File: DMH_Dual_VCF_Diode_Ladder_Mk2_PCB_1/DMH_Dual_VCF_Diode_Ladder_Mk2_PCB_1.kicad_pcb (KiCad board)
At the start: 2 copper layers, 146 x 175 mm, 201 parts, among them J0 Conn_01x01, J100 IDC_02x08, J50 Conn_01x06, J60 Conn_01x06, J70 Conn_01x06, J80 Conn_01x06, Q1 BC548, Q2 BC548, Q3 BC548, Q4 BC548, SW1 SW_SPDT, SW10 SW_DPDT_OnOn, SW2 SW_SPDT, SW3 SW_SPDT, SW4 SW_SPDT, SW5 SW_SPDT, SW6 SW_SPDT, SW7 SW_SPDT_OnOffOn, SW8 SW_SPDT_321, SW9 SW_SPDT_OnOffOn, U1 TL074, U2 TL074, U3 TL074, U4 TL074, U5 TL074, U6 TL074, U7 TL074

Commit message: PCB1 component placement in progress
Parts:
- removed D3: LED_Blue, LED_THT:LED_D3.0mm
- removed D4, D5: LED_Red, LED_THT:LED_D3.0mm
- removed J50, J60, J70, J80: Conn_01x06, Connector_PinSocket_2.54mm:PinSocket_1x06_P2.54mm_Vertical
- removed R1, R11, R16, R76: 100k, Resistor_THT:R_Axial_DIN0207_L6.3mm_D2.5mm_P7.62mm_Horizontal
- removed R10, R24, R25, R9: 47k, Resistor_THT:R_Axial_DIN0207_L6.3mm_D2.5mm_P7.62mm_Horizontal
- removed R12, R17, R2: 27k, Resistor_THT:R_Axial_DIN0207_L6.3mm_D2.5mm_P7.62mm_Horizontal
- removed R13, R14, R15: 3k3, Resistor_THT:R_Axial_DIN0207_L6.3mm_D2.5mm_P7.62mm_Horizontal
- removed R23, R8: 68k, Resistor_THT:R_Axial_DIN0207_L6.3mm_D2.5mm_P7.62mm_Horizontal
- removed R80: 20k, Resistor_THT:R_Axial_DIN0207_L6.3mm_D2.5mm_P7.62mm_Horizontal
- removed RV1, RV18, RV22, RV6, RV7: 100k, SynthStuff:Potentiometer_Alpha_RD901F-40-00D_Single_Vertical
- removed RV11, RV16, RV20, RV3, RV5, RV9: 100k, SynthStuff:Potentiometer_TT_P110KH1
- removed RV19: 100k, Potentiometer_THT:Potentiometer_Bourns_3296W_Vertical
- removed SW1, SW2, SW3, SW4, SW5, SW6: SW_SPDT, SynthStuff:Toggle_Switch_TE
- removed SW10: SW_DPDT_OnOn, SynthStuff:Toggle_Switch_2_Poles_TE
- removed SW7, SW9: SW_SPDT_OnOffOn, SynthStuff:Toggle_Switch_TE
- removed SW8: SW_SPDT_321, SynthStuff:Toggle_Switch_TE
- added C19: 100nF, Capacitor_THT:C_Disc_D4.3mm_W1.9mm_P5.00mm, B.Cu at (265.6, 117.3)
- added C20: 100nF, Capacitor_THT:C_Disc_D4.3mm_W1.9mm_P5.00mm, B.Cu at (265.6, 120.8)
- added C35: 100nF, Capacitor_THT:C_Disc_D4.3mm_W1.9mm_P5.00mm, B.Cu at (265.6, 124.2)
- added C36: 100nF, Capacitor_THT:C_Disc_D4.3mm_W1.9mm_P5.00mm, B.Cu at (265.6, 127.7)
- added J1: TS_Jack_6.35mm_Sw, SynthStuff:CUI_MJ-63052A, F.Cu at (33.5, 190.2)
- added J10: TS_Jack_6.35mm_Sw, SynthStuff:CUI_MJ-63052A, F.Cu at (150.0, 208.8)
- added J11: TS_Jack_6.35mm_Sw, SynthStuff:CUI_MJ-63052A, F.Cu at (133.5, 190.2)
- added J12: TS_Jack_6.35mm_Sw, SynthStuff:CUI_MJ-63052A, F.Cu at (133.5, 208.8)
- added J13: TS_Jack_6.35mm_Sw, SynthStuff:CUI_MJ-63052A, F.Cu at (117.0, 208.8)
- added J14: TS_Jack_6.35mm_Sw, SynthStuff:CUI_MJ-63052A, F.Cu at (166.5, 208.8)
- added J15: Conn_01x08_PinHeader, Connector_PinHeader_2.54mm:PinHeader_1x08_P2.54mm_Vertical, F.Cu at (30.0, 128.0)
- added J16: Conn_01x08_PinHeader, Connector_PinHeader_2.54mm:PinHeader_1x08_P2.54mm_Vertical, F.Cu at (170.0, 128.0)
- added J17: Conn_01x06_PinHeader, Connector_PinHeader_2.54mm:PinHeader_1x06_P2.54mm_Vertical, F.Cu at (30.0, 94.5)
- added J18: Conn_01x06_PinHeader, Connector_PinHeader_2.54mm:PinHeader_1x06_P2.54mm_Vertical, F.Cu at (170.0, 94.5)
- added J19: Conn_01x04_PinHeader, Connector_PinHeader_2.54mm:PinHeader_1x04_P2.54mm_Vertical, F.Cu at (98.0, 143.8)
- added J2: TS_Jack_6.35mm_Sw, SynthStuff:CUI_MJ-63052A, F.Cu at (50.0, 190.2)
- added J20: Conn_01x04_PinHeader, Connector_PinHeader_2.54mm:PinHeader_1x04_P2.54mm_Vertical, F.Cu at (102.0, 143.8)
- added J200: IDC_02x05, SynthStuff:IDC-Header_2x05_P2.54mm_Vertical_BackBone, B.Cu at (81.9, 192.2)
- added J21: Conn_01x06_PinHeader, Connector_PinHeader_2.54mm:PinHeader_1x06_P2.54mm_Vertical, F.Cu at (30.0, 56.5)
- added J210: IDC_02x05, SynthStuff:IDC-Header_2x05_P2.54mm_Vertical_BackBone, B.Cu at (108.0, 192.2)
- added J22: Conn_01x06_PinHeader, Connector_PinHeader_2.54mm:PinHeader_1x06_P2.54mm_Vertical, F.Cu at (170.0, 56.5)
- added J23: Conn_01x04_PinHeader, Connector_PinHeader_2.54mm:PinHeader_1x04_P2.54mm_Vertical, F.Cu at (96.2, 62.8)
- added J3: TS_Jack_6.35mm_Sw, SynthStuff:CUI_MJ-63052A, F.Cu at (50.0, 208.8)
- added J4: TS_Jack_6.35mm_Sw, SynthStuff:CUI_MJ-63052A, F.Cu at (66.5, 190.2)
- added J5: TS_Jack_6.35mm_Sw, SynthStuff:CUI_MJ-63052A, F.Cu at (66.5, 208.8)
- added J6: TS_Jack_6.35mm_Sw, SynthStuff:CUI_MJ-63052A, F.Cu at (83.0, 208.8)
- added J7: TS_Jack_6.35mm_Sw, SynthStuff:CUI_MJ-63052A, F.Cu at (33.5, 208.8)
- added J8: TS_Jack_6.35mm_Sw, SynthStuff:CUI_MJ-63052A, F.Cu at (166.5, 190.2)
- added J9: TS_Jack_6.35mm_Sw, SynthStuff:CUI_MJ-63052A, F.Cu at (150.0, 190.2)
- added Q5: BC548, Package_TO_SOT_THT:TO-92L_Inline_Wide, B.Cu at (297.4, 174.2)
- added Q6: BC548, Package_TO_SOT_THT:TO-92L_Inline_Wide, B.Cu at (297.5, 184.4)
- added Q7: BC548, Package_TO_SOT_THT:TO-92L_Inline_Wide, B.Cu at (254.5, 209.7)
- added Q8: BC548, Package_TO_SOT_THT:TO-92L_Inline_Wide, B.Cu at (254.7, 218.8)
- added R100: 10k, Resistor_THT:R_Axial_DIN0207_L6.3mm_D2.5mm_P7.62mm_Horizontal, B.Cu at (330.1, 170.2)
- added R101: 1k, Resistor_THT:R_Axial_DIN0207_L6.3mm_D2.5mm_P7.62mm_Horizontal, B.Cu at (330.1, 174.2)
- added R102: 10k, Resistor_THT:R_Axial_DIN0207_L6.3mm_D2.5mm_P7.62mm_Horizontal, B.Cu at (330.1, 178.2)
- added R103: 100k, Resistor_THT:R_Axial_DIN0207_L6.3mm_D2.5mm_P7.62mm_Horizontal, B.Cu at (330.1, 182.3)
- added R104: 33k, Resistor_THT:R_Axial_DIN0207_L6.3mm_D2.5mm_P7.62mm_Horizontal, B.Cu at (330.1, 186.3)
- added R105: 100k, Resistor_THT:R_Axial_DIN0207_L6.3mm_D2.5mm_P7.62mm_Horizontal, B.Cu at (319.4, 158.0)
- added R106: 100k, Resistor_THT:R_Axial_DIN0207_L6.3mm_D2.5mm_P7.62mm_Horizontal, B.Cu at (319.4, 162.1)
- added R107: 100k, Resistor_THT:R_Axial_DIN0207_L6.3mm_D2.5mm_P7.62mm_Horizontal, B.Cu at (319.4, 166.1)
- added R108: 100R, Resistor_THT:R_Axial_DIN0207_L6.3mm_D2.5mm_P7.62mm_Horizontal, B.Cu at (319.4, 170.2)
- added R109: 100R, Resistor_THT:R_Axial_DIN0207_L6.3mm_D2.5mm_P7.62mm_Horizontal, B.Cu at (319.4, 174.2)
- added R110: 10k, Resistor_THT:R_Axial_DIN0207_L6.3mm_D2.5mm_P7.62mm_Horizontal, B.Cu at (319.4, 178.2)
- added R112: 82k, Resistor_THT:R_Axial_DIN0207_L6.3mm_D2.5mm_P7.62mm_Horizontal, B.Cu at (319.4, 182.3)
- added R113: 100k, Resistor_THT:R_Axial_DIN0207_L6.3mm_D2.5mm_P7.62mm_Horizontal, B.Cu at (319.4, 186.3)
- added R114: 20k, Resistor_THT:R_Axial_DIN0207_L6.3mm_D2.5mm_P7.62mm_Horizontal, B.Cu at (287.3, 192.4)
- added R115: 20k, Resistor_THT:R_Axial_DIN0207_L6.3mm_D2.5mm_P7.62mm_Horizontal, B.Cu at (287.3, 196.4)
- added R116: 100k, Resistor_THT:R_Axial_DIN0207_L6.3mm_D2.5mm_P7.62mm_Horizontal, B.Cu at (287.3, 200.5)
- added R117: 10k, Resistor_THT:R_Axial_DIN0207_L6.3mm_D2.5mm_P7.62mm_Horizontal, B.Cu at (287.3, 204.6)
- added R118: 1k, Resistor_THT:R_Axial_DIN0207_L6.3mm_D2.5mm_P7.62mm_Horizontal, B.Cu at (287.3, 208.6)
- added R119: 10k, Resistor_THT:R_Axial_DIN0207_L6.3mm_D2.5mm_P7.62mm_Horizontal, B.Cu at (287.3, 212.7)
- added R120: 100k, Resistor_THT:R_Axial_DIN0207_L6.3mm_D2.5mm_P7.62mm_Horizontal, B.Cu at (287.3, 216.7)
- added R121: 33k, Resistor_THT:R_Axial_DIN0207_L6.3mm_D2.5mm_P7.62mm_Horizontal, B.Cu at (287.3, 220.8)
- added R122: 100k, Resistor_THT:R_Axial_DIN0207_L6.3mm_D2.5mm_P7.62mm_Horizontal, B.Cu at (276.5, 192.4)
- added R123: 100k, Resistor_THT:R_Axial_DIN0207_L6.3mm_D2.5mm_P7.62mm_Horizontal, B.Cu at (276.5, 196.4)
- added R124: 100k, Resistor_THT:R_Axial_DIN0207_L6.3mm_D2.5mm_P7.62mm_Horizontal, B.Cu at (276.5, 200.5)
- added R125: 100R, Resistor_THT:R_Axial_DIN0207_L6.3mm_D2.5mm_P7.62mm_Horizontal, B.Cu at (276.5, 204.6)
- added R126: 100R, Resistor_THT:R_Axial_DIN0207_L6.3mm_D2.5mm_P7.62mm_Horizontal, B.Cu at (276.5, 208.6)
- added R127: 10k, Resistor_THT:R_Axial_DIN0207_L6.3mm_D2.5mm_P7.62mm_Horizontal, B.Cu at (276.5, 212.7)
- added R129: 82k, Resistor_THT:R_Axial_DIN0207_L6.3mm_D2.5mm_P7.62mm_Horizontal, B.Cu at (276.5, 216.7)
- added R130: 100k, Resistor_THT:R_Axial_DIN0207_L6.3mm_D2.5mm_P7.62mm_Horizontal, B.Cu at (276.5, 220.8)
- added R97: 20k, Resistor_THT:R_Axial_DIN0207_L6.3mm_D2.5mm_P7.62mm_Horizontal, B.Cu at (330.1, 158.0)
- added R98: 20k, Resistor_THT:R_Axial_DIN0207_L6.3mm_D2.5mm_P7.62mm_Horizontal, B.Cu at (330.1, 162.1)
- added R99: 100k, Resistor_THT:R_Axial_DIN0207_L6.3mm_D2.5mm_P7.62mm_Horizontal, B.Cu at (330.1, 166.1)
- added RV24: 50k, Potentiometer_THT:Potentiometer_Bourns_3296W_Vertical, B.Cu at (302.1, 176.0)
- added RV26: 100k, Potentiometer_THT:Potentiometer_Bourns_3296W_Vertical, B.Cu at (302.1, 185.2)
- added RV29: 100k, Potentiometer_THT:Potentiometer_Bourns_3296W_Vertical, B.Cu at (259.2, 219.6)
- added U10: TL074, Package_DIP:DIP-14_W7.62mm_Socket, B.Cu at (153.8, 93.1)
- added U8: TL074, Package_DIP:DIP-14_W7.62mm_Socket, B.Cu at (153.8, 131.1)
- added U9: TL074, Package_DIP:DIP-14_W7.62mm_Socket, B.Cu at (53.8, 93.1)
- R62: value 33k -> 20k
- R65, R67: value 100k -> 10k
- R66: value 82k -> 1k
- R68, R70: value 100R -> 100k
- R69: value 10k -> 33k
- R72: value 20k -> 100k
- R73: value 20k -> 100R
- R74: value 10k -> 100R
- R77: value 100k -> 82k
- R78: value 1k -> 100k
- RV12, RV14: value 100k -> 50k; footprint SynthStuff:Potentiometer_Alpha_RD901F-40-00D_Single_Vertical -> Potentiometer_THT:Potentiometer_Bourns_3296W_Vertical; moved to B.Cu
- RV17: value 50k -> 100k
- moved D23 282.8 mm to (384.7, 59.2), turned to 180 degrees
- moved D22 280.9 mm to (384.7, 54.9), turned to 180 degrees
- moved D15 273.7 mm to (384.7, 24.7), turned to 180 degrees
- moved R48 263.4 mm to (373.9, 41.1), turned to 180 degrees
- moved R58 261.5 mm to (352.4, 33.0), turned to 180 degrees
- moved R46 261.2 mm to (373.9, 33.0)
- moved D7 260.5 mm to (285.1, 62.5), turned to 180 degrees
- moved R47 258.6 mm to (373.9, 37.1), turned to 180 degrees
- moved D8 256.7 mm to (285.1, 66.8), turned to 180 degrees
- moved C34 253.8 mm to (373.9, 69.6), turned to 180 degrees
- moved D9 252.9 mm to (285.1, 71.2), turned to 180 degrees
- moved R61 250.9 mm to (352.4, 45.2), turned to 180 degrees
- moved D10 249.2 mm to (285.1, 75.5), turned to 180 degrees
- moved R56 248.8 mm to (352.4, 24.9), turned to 180 degrees
- moved R52 246.6 mm to (363.1, 33.0), turned to 180 degrees
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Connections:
- net /CV Processing/Bus CV A Input renamed /Inputs and Outputs A/CV 3 TN
- C21 pad 1: Net-(C21-Pad1) -> /Core Circuit A/Input
- C28 pad 1: Net-(C28-Pad1) -> /Core Circuit B/Input
- D15 pad 2: /CV Processing/Link Switch -> /CV Processing/Link CV Switch
- R18 pad 2: Net-(U7A--) -> Net-(U8A--)
- R19 pad 2: Net-(U5B--) -> Net-(J16A-Pin_1)
- R20 pad 1: Net-(U5B--) -> Net-(J16A-Pin_1)
- R21 pad 2: Net-(U7B--) -> Net-(U8B--)
- R22 pad 2: Net-(U5B--) -> Net-(J16A-Pin_1)
- R4 pad 2: Net-(U5B--) -> Net-(J15A-Pin_1)
- R5 pad 1: Net-(U5B--) -> Net-(J15A-Pin_1)
- R62 pad 1: /Inputs and Outputs A/Res CV Jack -> Net-(Q1-C)
- R62 pad 2: Net-(U1D--) -> +12V
- R63 pad 1: Net-(R63-Pad1) -> Net-(Q2-C)
- R64 pad 2: Net-(U1B--) -> Net-(U1C--)
- R65 pad 1: Net-(R65-Pad1) -> Net-(U1C--)
- R65 pad 2: Net-(U1B--) -> Net-(Q1-C)
- R66 pad 1: Net-(U1B--) -> /Core Circuit A/Res Input
- R66 pad 2: Net-(R66-Pad2) -> Net-(R64-Pad1)
- R67 pad 1: Net-(Q1-B) -> Net-(U1C-+)
- R67 pad 2: /Core Circuit A/Raw Output -> Net-(Q2-C)
- R68 pad 1: GND -> Net-(U1C-+)
- R68 pad 2: Net-(Q1-B) -> GND
- R69 pad 1: Net-(R66-Pad2) -> /Inputs and Outputs A/Res CV Jack
- R69 pad 2: Net-(Q1-E) -> Net-(U1D--)
- R7 pad 2: Net-(U5B--) -> Net-(J15A-Pin_1)
- R70 pad 1: GND -> Net-(R70-Pad1)
- R70 pad 2: Net-(Q2-B) -> Net-(U1B--)
- R71 pad 1: Net-(R71-Pad1) -> Net-(Q1-B)
- R71 pad 2: Net-(Q2-B) -> /Core Circuit A/Raw Output
- R72 pad 1: Net-(Q1-C) -> Net-(R72-Pad1)
- R72 pad 2: +12V -> Net-(Q2-B)
- R73 pad 1: Net-(Q2-C) -> GND
- R73 pad 2: +12V -> Net-(Q1-B)
- R74 pad 1: Net-(U1C--) -> GND
- R74 pad 2: Net-(Q1-C) -> Net-(Q2-B)
- R75 pad 1: Net-(U1C-+) -> /Resonance A CV/Res CV
- R75 pad 2: Net-(Q2-C) -> Net-(Q1-E)
- R77 pad 1: Net-(R77-Pad1) -> Net-(U1B--)
- R77 pad 2: Net-(U1C--) -> /Resonance A CV/Res CV
- R78 pad 1: /Core Circuit A/Res Input -> Net-(J21C-Pin_3)
- R78 pad 2: Net-(R77-Pad1) -> Net-(U1B--)
- R83 pad 2: Net-(R83-Pad2) -> Net-(J22D-Pin_4)
- R86 pad 1: Net-(R83-Pad2) -> Net-(J22F-Pin_6)
- RV10 pad 1: Net-(U7B--) -> Net-(U8B--)
- RV12 pad 1: GND -> Net-(U10A--)
- RV12 pad 2: Net-(C21-Pad1) -> Net-(R122-Pad1)
- RV12 pad 3: /Core Circuit A/Input -> Net-(R122-Pad1)
- RV14 pad 1: GND -> Net-(U1D--)
- RV14 pad 2: Net-(C28-Pad1) -> Net-(R70-Pad1)
- RV14 pad 3: /Core Circuit B/Input -> Net-(R70-Pad1)
- RV17 pad 1: Net-(U1D--) -> -12V
- RV17 pad 2: Net-(R64-Pad1) -> Net-(R72-Pad1)
- RV17 pad 3: Net-(R64-Pad1) -> +12V
- RV8 pad 1: Net-(U7A--) -> Net-(U8A--)
- U1 pad 14: Net-(R64-Pad1) -> Net-(R70-Pad1)
- U1 pad 7: Net-(R66-Pad2) -> /Resonance A CV/Res CV
- U1 pad 8: Net-(R77-Pad1) -> Net-(R64-Pad1)
- U2 pad 8: Net-(R83-Pad2) -> Net-(J22D-Pin_4)
- U5 pad 7: /CV Processing/CV A -> Net-(U5B--)
- U6 pad 8: /CV Processing/CV B -> Net-(U6C--)
- U6 pad 9: Net-(U5B--) -> Net-(U6C--)
- U7 pad 1: Net-(R19-Pad1) -> /CV Processing/CV A
- U7 pad 2: Net-(U7A--) -> Net-(J15A-Pin_1)
- U7 pad 3: Net-(U7A-+) -> GND
- U7 pad 5: Net-(U7B-+) -> GND
- U7 pad 7: Net-(R22-Pad1) -> Net-(U7B--)
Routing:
- net +12V: track 550.6 -> 44.1 mm
- net -12V: track 494.0 -> 59.8 mm
- net Net-(U5B--): track 360.9 -> 0.00 mm
- net /Inputs and Outputs A/Res CV Jack: track 247.6 -> 4.71 mm
- net /Inputs and Outputs A/CV 3 TN: track 177.2 -> 2.54 mm
- net /Inputs and Outputs B/Res CV Jack: track 150.2 -> 0.00 mm
- net /Core Circuit A/Input: track 148.9 -> 0.00 mm
- net /CV Processing/CV2 A Input: track 147.5 -> 0.00 mm
- net Net-(D13-A): track 146.9 -> 0.00 mm
- net Net-(J22B-Pin_2): track 128.7 -> 0.00 mm
- net /CV Processing/CV B: track 117.8 -> 0.00 mm
- net /CV Processing/CV1 A Input: track 117.1 -> 0.00 mm
- net /CV Processing/Link Switch: track 115.9 -> 0.00 mm
- net /Core Circuit A/Output: track 113.9 -> 0.00 mm
- net /Core Circuit B/Output: track 113.8 -> 0.00 mm
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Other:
- outline, holes or cut-outs redrawn
- board text removed: "Mk1.0 - Month Year"

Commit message: Routed one half
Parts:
- moved R104 308.2 mm to (34.2, 100.2), turned to 0 degrees
- moved R103 307.8 mm to (29.2, 117.3), turned to 90 degrees
- moved R98 297.8 mm to (34.2, 128.5), turned to 0 degrees
- moved R113 297.0 mm to (34.2, 103.5), turned to 0 degrees
- moved R102 295.1 mm to (41.8, 115.5)
- moved R99 293.3 mm to (41.8, 112.2)
- moved R100 292.9 mm to (41.8, 118.8)
- moved R109 289.4 mm to (34.2, 125.2), turned to 0 degrees
- moved R107 288.6 mm to (34.2, 122.0), turned to 0 degrees
- moved R105 281.6 mm to (46.2, 89.5), turned to 0 degrees
- moved RV24 278.9 mm to (35.5, 94.2)
- moved R97 273.8 mm to (58.7, 122.0), turned to 0 degrees
- moved R110 272.0 mm to (53.8, 119.5)
- moved RV26 270.3 mm to (47.5, 94.2)
- moved R101 268.3 mm to (66.3, 125.2)
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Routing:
- net +12V: track 44.1 -> 404.0 mm
- net /Inputs and Outputs A/Res CV Jack: track 4.71 -> 243.3 mm
- net /Drive A/Input: track 0.00 -> 231.6 mm
- net -12V: track 59.8 -> 282.7 mm
- net /Drive A/Drive CV Input: track 0.00 -> 214.7 mm
- net /CV Processing/CV1 A Input: track 0.00 -> 186.1 mm
- net /CV Processing/CV2 A Input: track 0.00 -> 159.4 mm
- net /Core Circuit A/Output: track 0.00 -> 148.9 mm
- net /Inputs and Outputs A/CV 3 TN: track 2.54 -> 140.1 mm
- net Net-(D13-A): track 0.00 -> 114.6 mm
- net Net-(D10-A): track 0.00 -> 75.7 mm
- net /CV Processing/CV3 A Input: track 0.00 -> 74.6 mm
- net Net-(R107-Pad1): track 0.00 -> 65.1 mm
- net Net-(J19C-Pin_3): track 0.00 -> 64.9 mm
- net Net-(J19D-Pin_4): track 0.00 -> 62.8 mm
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
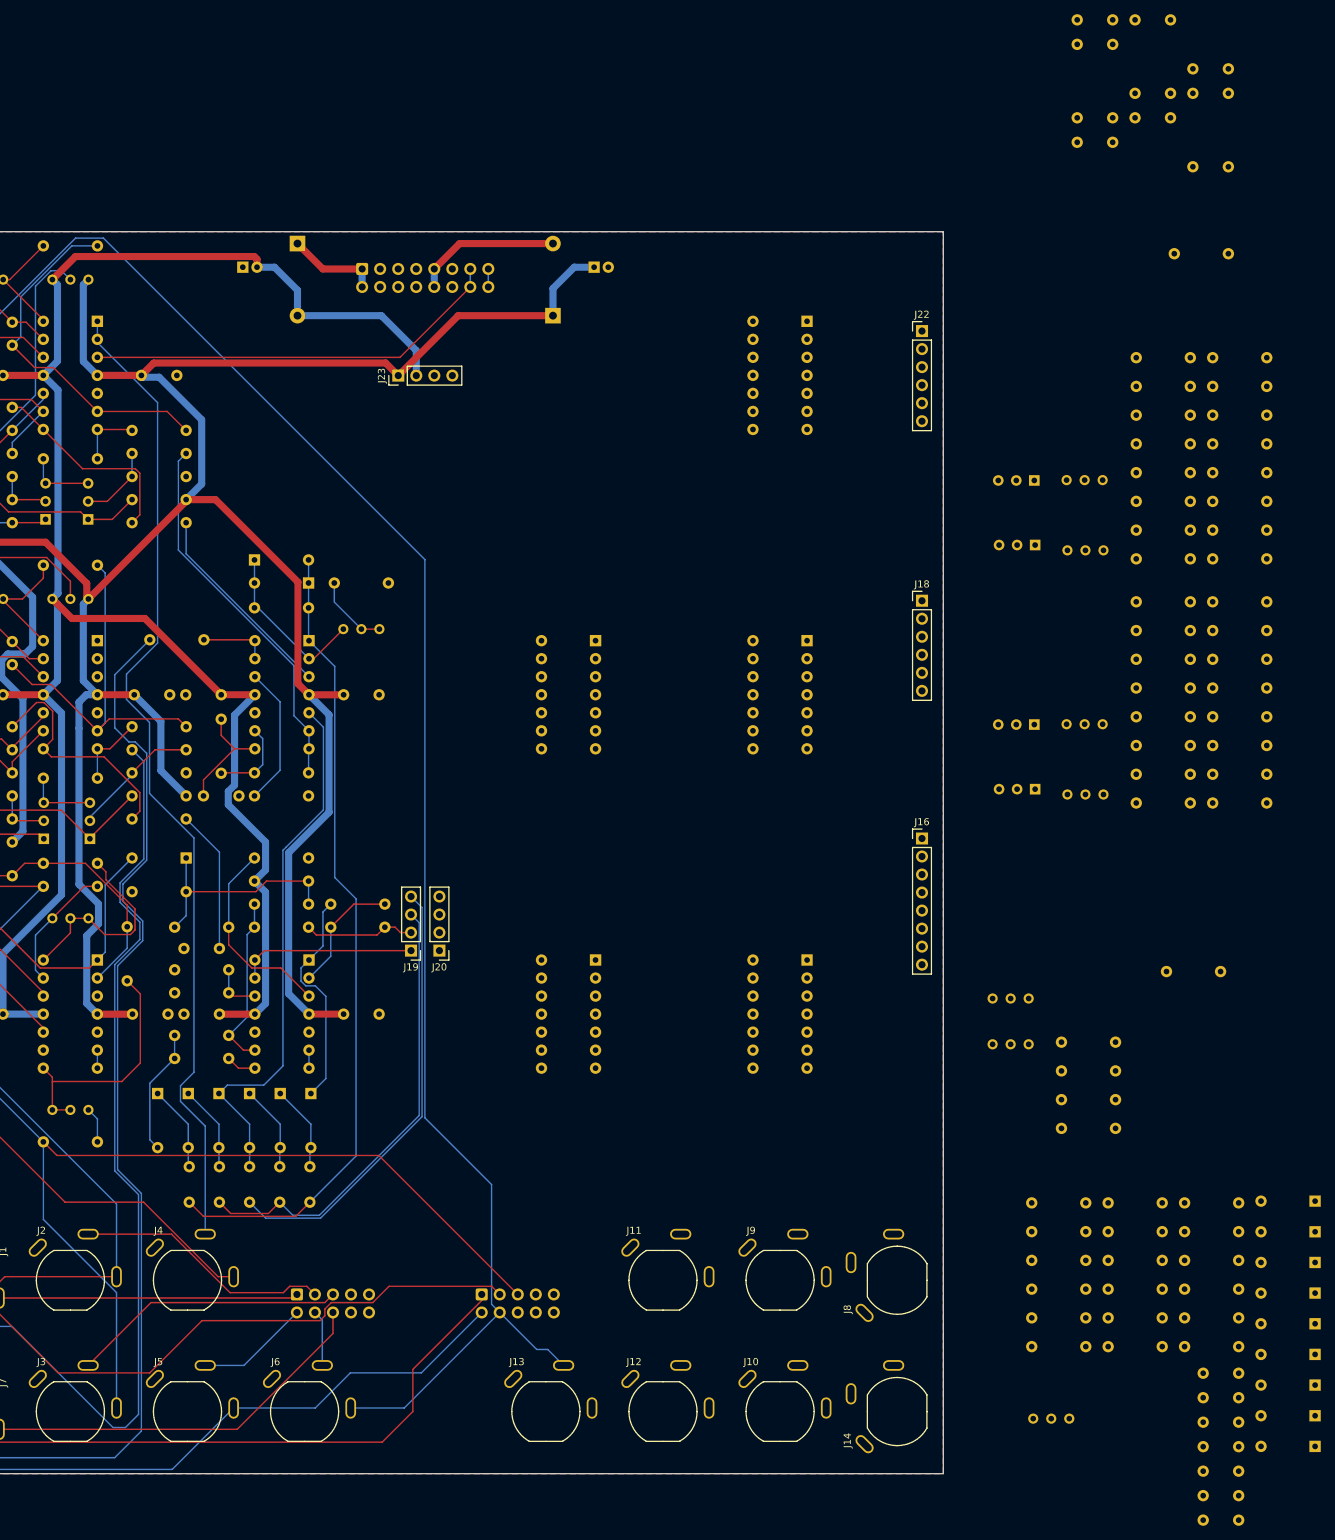
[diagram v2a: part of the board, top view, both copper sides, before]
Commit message: Placed components on circuit B
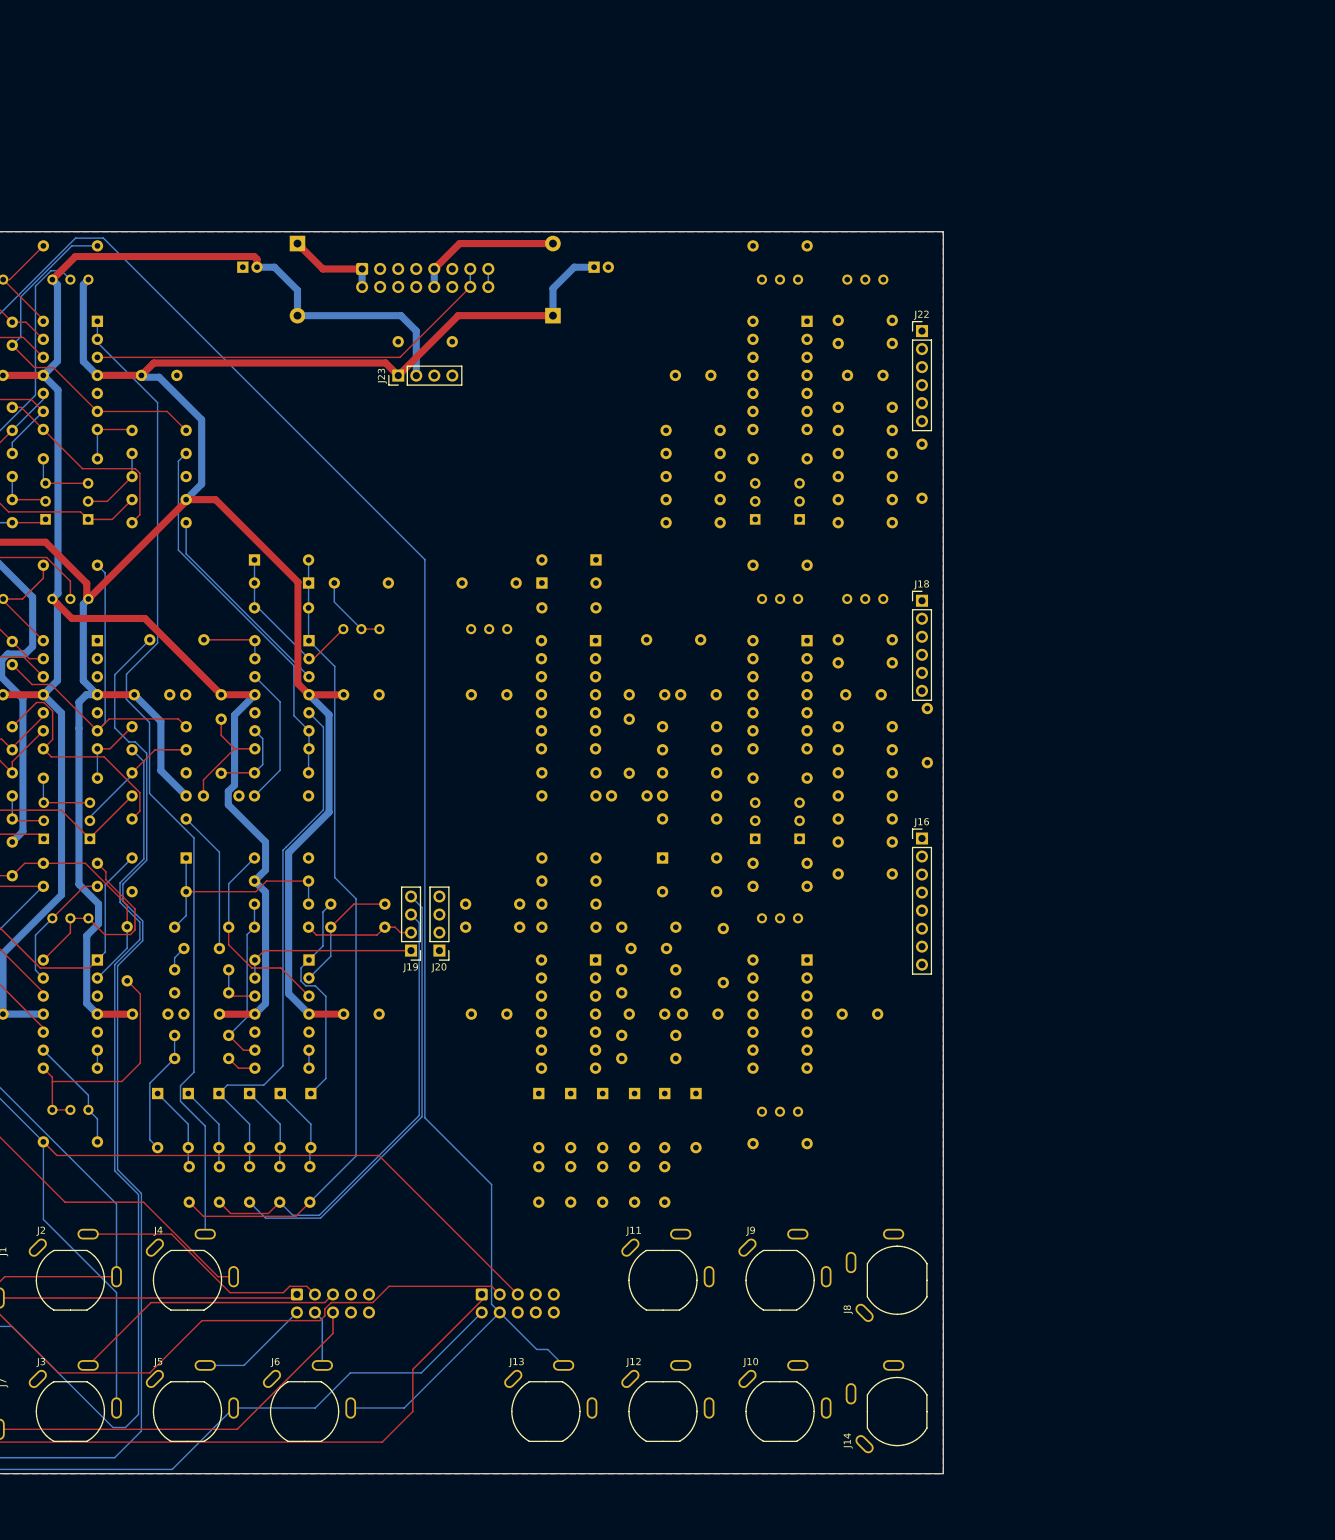
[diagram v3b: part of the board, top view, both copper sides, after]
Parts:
- moved D23 160.8 mm to (124.1, 88.8)
- moved C14 160.2 mm to (106.5, 152.8), turned to 0 degrees
- moved D22 160.1 mm to (116.4, 92.0), turned to 0 degrees
- moved C13 150.5 mm to (128.8, 152.8), turned to 0 degrees
- moved C18 149.5 mm to (136.2, 152.8), turned to 0 degrees
- moved C17 145.2 mm to (158.8, 152.8), turned to 0 degrees
- moved C10 136.9 mm to (106.5, 107.8), turned to 0 degrees
- moved RV15 133.7 mm to (111.5, 98.5), turned to 0 degrees
- moved C34 131.8 mm to (131.2, 122.0)
- moved R58 124.7 mm to (112.8, 92.0)
- moved R96 117.6 mm to (96.2, 58.0), turned to 0 degrees
- moved R61 117.3 mm to (131.2, 100.0), turned to 0 degrees
- moved D21 116.8 mm to (116.0, 163.9), turned to -90 degrees
- moved R54 114.2 mm to (105.7, 137.2), turned to 0 degrees
- moved C9 112.5 mm to (128.8, 107.8), turned to 0 degrees
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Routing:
- net Net-(U7C--): track 5.03 -> 16.1 mm
- net Net-(C21-Pad2): track 0.00 -> 3.54 mm
- net -12V: track 282.7 -> 284.3 mm
